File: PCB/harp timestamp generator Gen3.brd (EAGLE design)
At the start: 124.5 x 80.4 mm, 144 parts, among them IC1 MCP73831T-2ATI/OT, IC10 SN74LVC1G125DBVT, IC11 TLV70033DDCR, IC12 SI8621BC-B-IS, IC13 SI8621BC-B-IS, IC14 SI8621BC-B-IS, IC15 SI8621BC-B-IS, IC16 SI8621BC-B-IS, IC17 SI8621BC-B-IS, IC18 SN74LVC1G125DBVT, IC19 SN74LVC1G125DBVT, IC2 USBLC6-2SC6, IC3 FT232RL, IC4 ICL7673CBAZA-T, IC5 TLV70033DDCR, IC6 ATXMEGA16A4U-AU, IC7 M74VHC1GT126DF1G, IC8 M74VHC1GT126DF1G, IC9 M74VHC1GT126DF1G, Q1 RTU002P02T106, Q2 BC817-40W, Q3 BC817-40LT1SMD, Q4 DMG1012UW, Q5 DMP2035U-7, T1 BC850, T10 BC850, T2 BC850, T3 BC850, T4 BC850, T5 BC850, T6 BC850, T7 BC850, T8 BC850, T9 BC850, X1 B2B-PH-K-S(LF)(SN), X2 B2B-PH-K-S(LF)(SN)

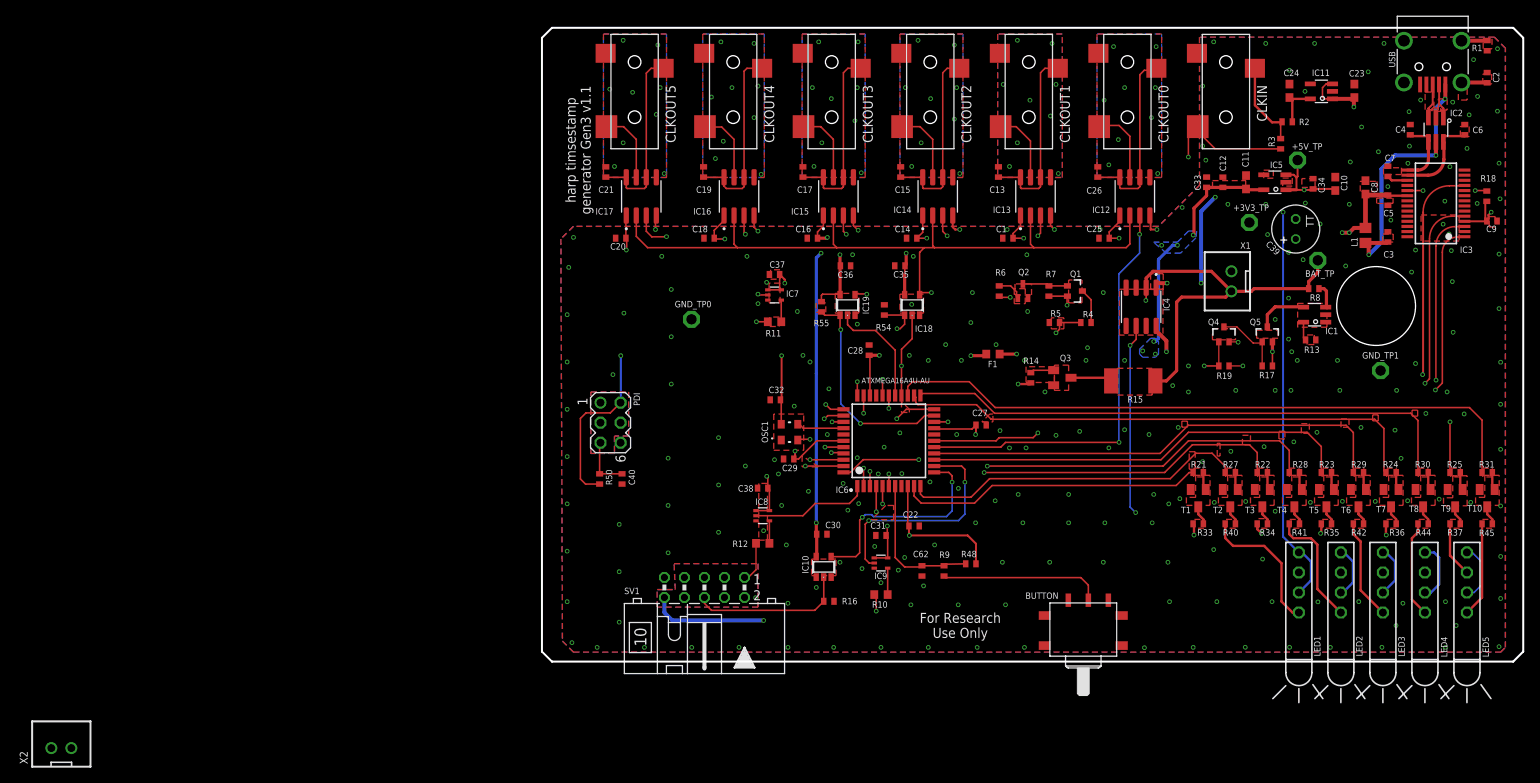
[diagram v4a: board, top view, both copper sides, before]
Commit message: Changed battery connection to a new location and added an ON/OFF button.
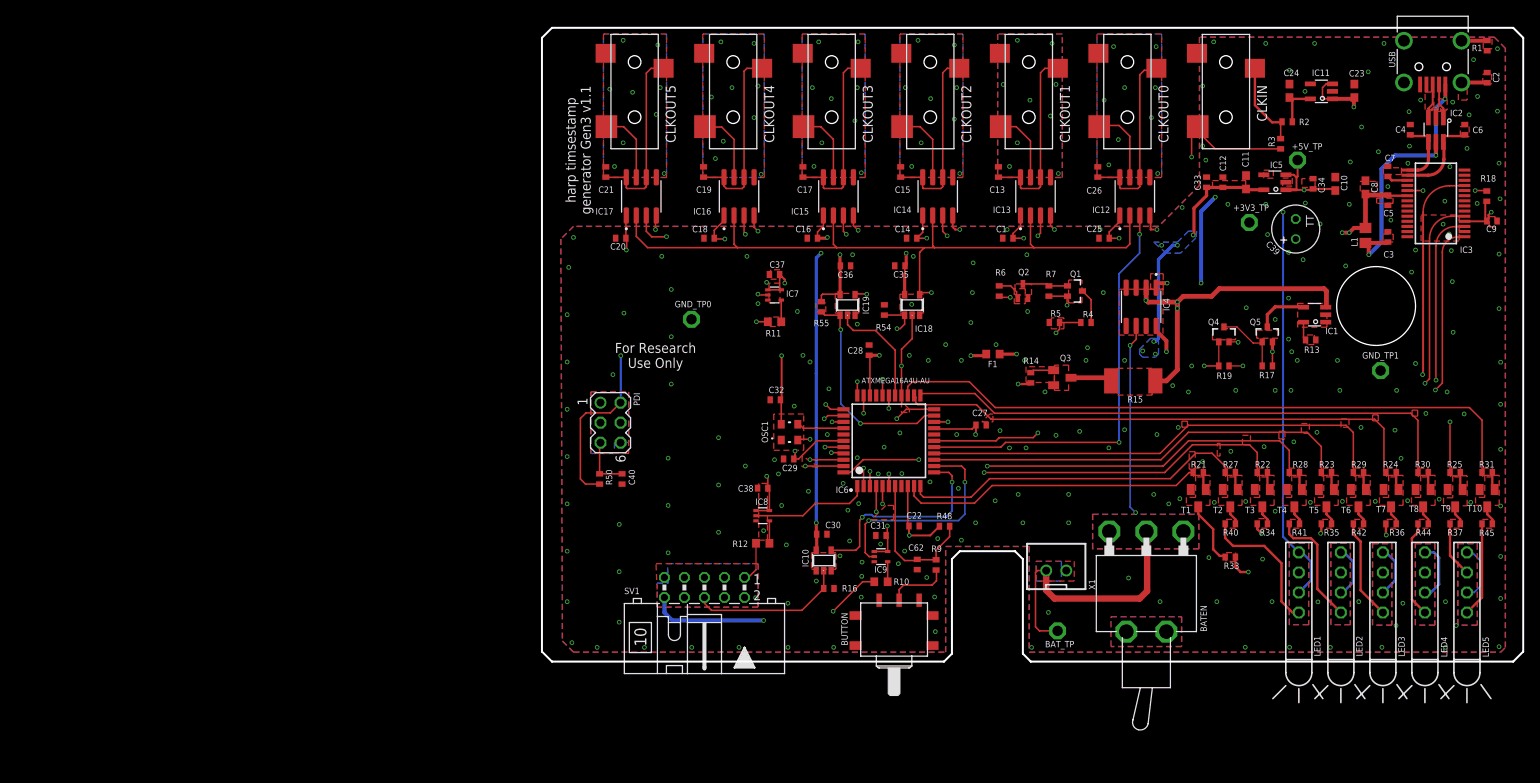
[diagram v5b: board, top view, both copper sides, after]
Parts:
- removed R8: 0, rcl:R0402
- removed X2: B2B-PH-K-S(LF)(SN), harp timestamp generator:JST-XH-02-PACKAGE-ROUND-PAD
- added BATEN: 100-SP3, cyclops:2M1-SP1-T2-B4-M6RE
- moved BAT_TP 57.4 mm to (65.4, 3.89)
- moved X1 42.9 mm to (65.2, 11.5), turned to 0 degrees
- moved BUTTON 24.0 mm to (44.7, 3.94)
- moved R33 5.85 mm to (87.3, 13.3), turned to 180 degrees
- moved R48 5.82 mm to (51.1, 17.2), turned to 180 degrees
- moved R10 1.63 mm to (43.0, 10.1)
- moved R16 1.63 mm to (36.4, 9.27)
- moved R9 1.26 mm to (50.0, 12.3)
- moved C62 1.01 mm to (47.6, 12.3)
- moved IC10 0.81 mm to (35.7, 12.8)
- moved IC9 0.81 mm to (43.0, 13.3)
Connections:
- removed net N$97: IC1.3, R8.1
- new net N$82: BATEN.2, BAT_TP.TP, X1.1
- net V_BATT: now also BATEN.1, IC1.3; no longer BAT_TP.TP, R8.2, X1.1
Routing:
- net N$82: track 0.00 -> 35.1 mm
- net V_BATT: track 62.3 -> 86.7 mm, vias 2 -> 4
- net N$43: track 20.7 -> 7.93 mm
- net N$30: track 16.7 -> 9.59 mm
- net VDD: track 162.5 -> 155.4 mm
- net N$19: track 2.42 -> 8.35 mm
- net N$97: track 3.16 -> 0.00 mm
- net CLOCK_IN: track 90.0 -> 91.1 mm
- net TX: track 23.0 -> 22.0 mm
- net +5V: track 204.5 -> 203.7 mm
- net UC_TX: track 28.7 -> 27.9 mm
- net UC_RX: track 27.3 -> 26.5 mm
- net N$4: track 3.35 -> 2.54 mm
- net +3V3: track 354.4 -> 353.6 mm
- net N$31: track 14.2 -> 13.6 mm
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- added copper zone on layer 1, net N$115
- added copper zone on layer 1, net N$122
- added copper zone on layer 16, net N$84
- added copper zone on layer 15, net N$97
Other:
- outline, holes or cut-outs redrawn
- board text added: "BATEN"

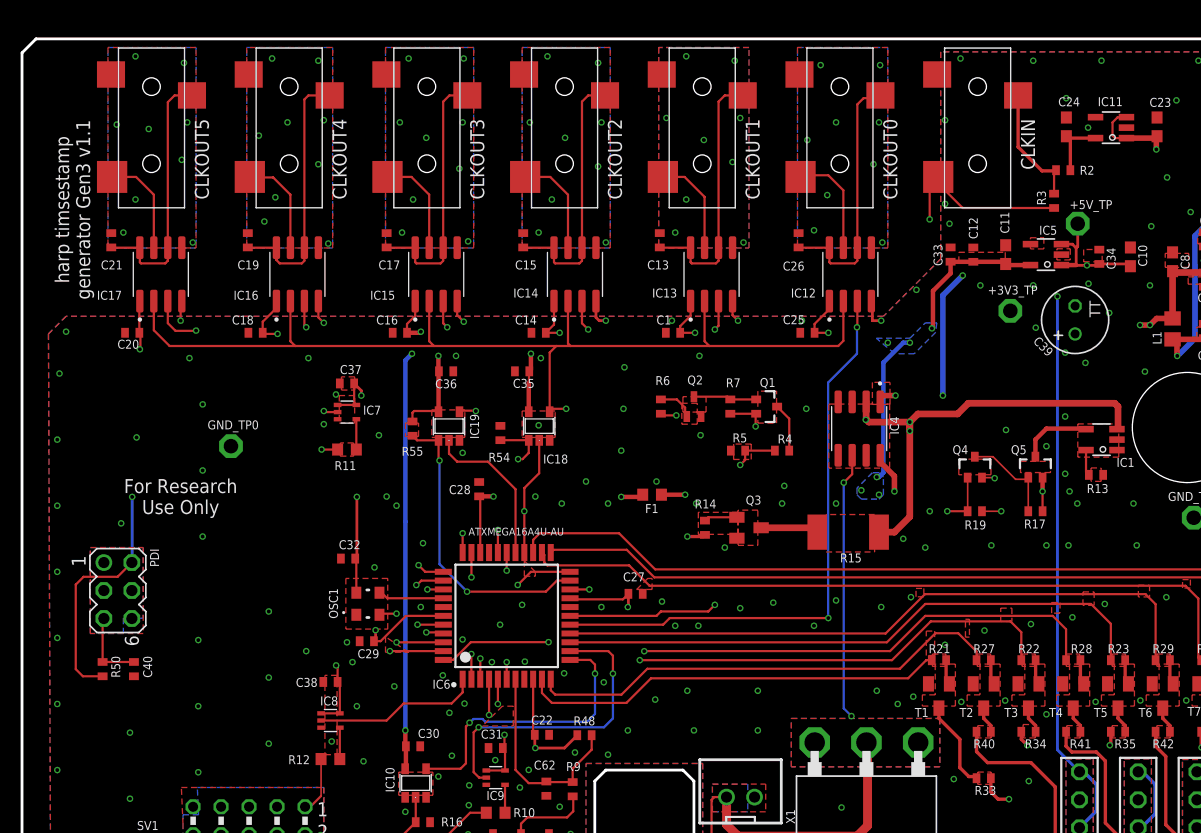
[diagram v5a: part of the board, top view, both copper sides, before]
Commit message: Added a new power switcher.
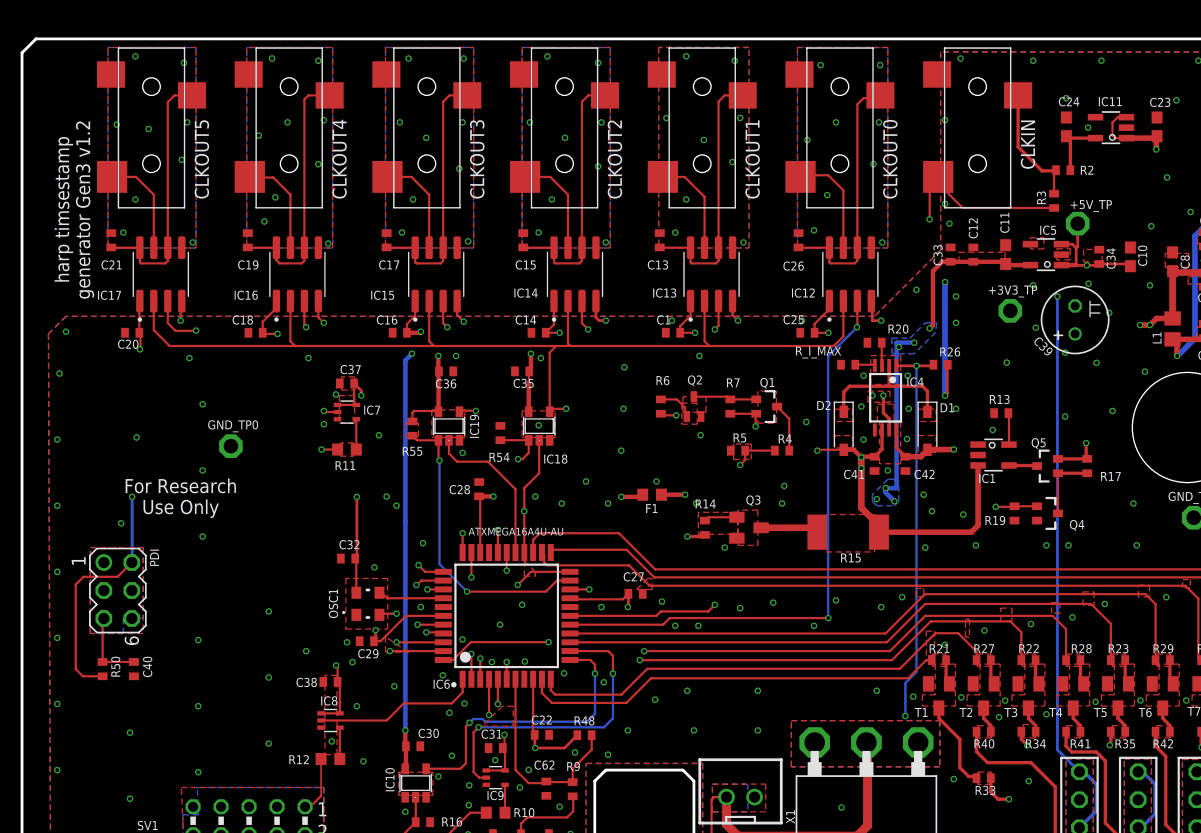
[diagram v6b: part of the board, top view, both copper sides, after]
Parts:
- added C41, C42: 100nF, rcl:C0402
- added D1, D2: DNI, harp timestamp generator Gen3:SOD3715X135
- added R20: 0R, rcl:R0402
- added R26: DNI, rcl:R0402
- added R_I_MAX: 1k, rcl:R0402
- BUTTON: device harp timestamp generator:CFPA -> harp timestamp generator Gen3:CFPA
- C33, C34: value 10n -> 10nF
- CLKIN, CLKOUT0, CLKOUT1, CLKOUT2, CLKOUT3, CLKOUT4, CLKOUT5: device harp timestamp generator:35RASMT2BHNTRX -> harp timestamp generator Gen3:35RASMT2BHNTRX
- F1: device harp timestamp generator:R0603 -> harp timestamp generator Gen3:R0603
- IC1: value MCP73831T-2ATI/OT -> MCP73831; device harp timestamp generator:TSOT23-5 -> harp timestamp generator Gen3:TSOT23-5
- IC11, IC5: device harp timestamp generator:TSOT23-5 -> harp timestamp generator Gen3:TSOT23-5
- IC12, IC13, IC14, IC15, IC16, IC17: value SI8621BC-B-IS -> SI8621BC; device harp timestamp generator:SOIC8 -> harp timestamp generator Gen3:SOIC8
- IC2: device harp timestamp generator:SOT23-6L -> harp timestamp generator Gen3:SOT23-6L
- IC3: value FT232RL -> FTDI232; device harp timestamp generator:SSOP28 -> harp timestamp generator Gen3:SSOP28
- IC4: value ICL7673CBAZA-T -> TPS2114; device harp timestamp generator:SOIC8 -> harp timestamp generator Gen3:TSSOP8
- IC6: device harp timestamp generator:QFP80P1200X1200X120-44N -> harp timestamp generator Gen3:QFP80P1200X1200X120-44N
- LED1, LED2, LED3, LED4, LED5: value 569-0112-100 -> LED-2HI; device harp timestamp generator:569-011X-X00_LED_ARRAY -> harp timestamp generator Gen3:569-011X-X00_LED_ARRAY
- OSC1: value OSCILLATOR -> OSC 32MHZ; device harp timestamp generator:OSCILLATOR_3.2X2.5 -> harp timestamp generator Gen3:OSCILLATOR_3.2X2.5
- Q1, Q4, Q5: device harp timestamp generator:SOT323 -> harp timestamp generator Gen3:SOT323
- Q3: value BC817-40LT1SMD -> SBC817; device transistor-npn:SOT23-BEC -> harp timestamp generator Gen3:SOT23-BEC
- R5: value 15K 0.1% => 14k7 -> 14k7
- R6: value 100k -> 14k7
- SV1: device harp timestamp generator:ML10L -> harp timestamp generator Gen3:ML10L
- T1, T10, T2, T3, T4, T5, T6, T7, T8, T9: device transistor:SOT23 -> harp timestamp generator Gen3:SOT23
- USB: device harp timestamp generator:240-0002-1 -> harp timestamp generator Gen3:240-0002-1
- X1: device harp timestamp generator:JST-XH-02-PACKAGE-ROUND-PAD -> harp timestamp generator Gen3:JST-XH-02-PACKAGE-ROUND-PAD
- moved R13 10.3 mm to (88.9, 46.4), turned to 0 degrees
- moved IC1 9.90 mm to (88.2, 42.6), turned to 270 degrees
- moved Q4 7.82 mm to (93.1, 37.3), turned to 270 degrees
- moved R17 6.24 mm to (96.7, 41.6), turned to 90 degrees
- moved IC4 3.69 mm to (78.4, 47.8), turned to 270 degrees
- moved R19 3.61 mm to (90.1, 37.3), turned to 90 degrees
- moved Q5 1.10 mm to (93.1, 41.6), turned to 90 degrees
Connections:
- new net N$114: IC4.4, R_I_MAX.1
- new net N$139: D1.1, D2.1, IC4.2
- new net N$140: IC4.3, R20.2
- net +5V: now also IC4.7, R26.1; no longer IC4.1
- net +5_USB: now also C42.1, D1.2
- net GND: now also C41.2, C42.2, IC4.5, R20.1, R_I_MAX.2; no longer IC4.4
- net PWR_GOOD: now also IC4.1, R26.2; no longer IC4.6
- net V_BATT: now also C41.1, D2.2, IC4.6; no longer IC4.2
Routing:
- net V_BATT: track 86.7 -> 69.0 mm
- net PWR_GOOD: track 60.5 -> 76.7 mm
- net N$139: track 0.00 -> 13.6 mm
- net CHARGE_ENABLE: track 63.1 -> 71.3 mm
- net +3V3: track 353.6 -> 359.9 mm
- net +5V: track 203.7 -> 208.7 mm, vias 11 -> 12
- net N$10: track 6.58 -> 2.57 mm
- net +5_USB: track 56.8 -> 53.2 mm, vias 5 -> 4
- net GND: track 17.8 -> 14.9 mm, vias 221 -> 227
- net N$2: track 8.75 -> 6.30 mm
- net N$140: track 0.00 -> 2.09 mm
- net N$114: track 0.00 -> 1.81 mm
- net N$16: track 2.36 -> 2.87 mm
- added copper zone on layer 1, net +5V
- added copper zone on layer 1, net N$141
- added copper zone on layer 1, net N$142
- removed copper zone on layer 1, net N$39
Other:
- board text added: "harp timsestamp generator Gen3 v1.2"
- board text removed: "harp timsestamp generator Gen3 v1.1"
